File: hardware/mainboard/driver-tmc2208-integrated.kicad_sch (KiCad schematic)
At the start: 11 parts, among them M1 JST XH, U7 TMC2208-LA

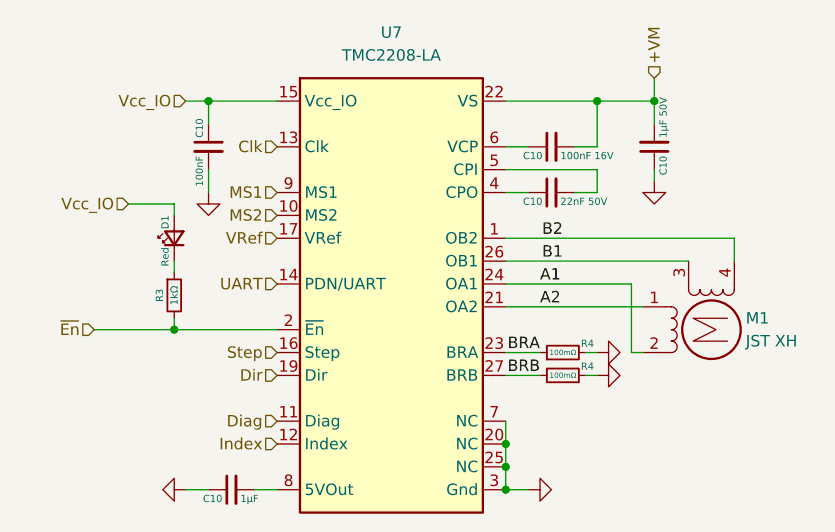
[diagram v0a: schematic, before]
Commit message: this is immediately before i switch the terminus USB hub with the corechips
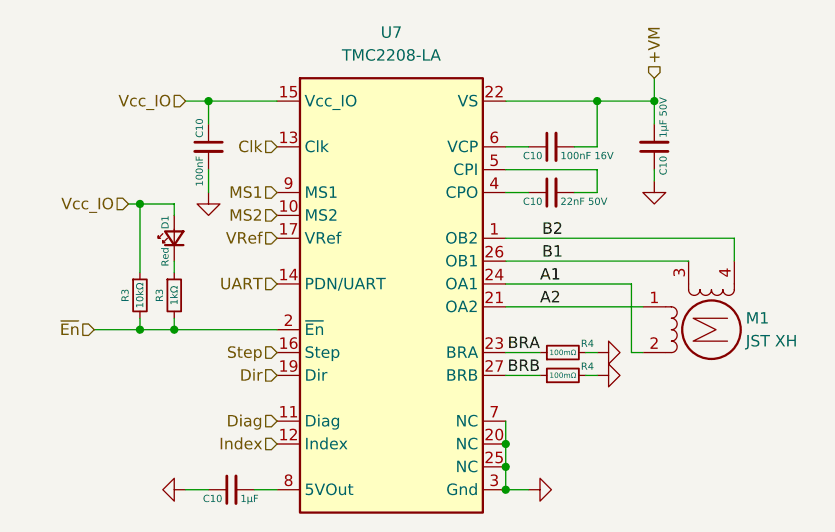
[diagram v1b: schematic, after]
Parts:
- added R3: 10kΩ, AlphaLib:0402R, symbol Device:R_Small
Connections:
- net Vcc_IO: now also R3.1
- net ~{En}: now also R3.2
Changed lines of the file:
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@@
   (junction (at 88.9 39.37) (diameter 0) (color 0 0 0 0)
   )
+  (junction (at 31.75 64.77) (diameter 0) (color 0 0 0 0)
+  )
   (junction (at 82.55 39.37) (diameter 0) (color 0 0 0 0)
   )
@@
   (junction (at 72.39 82.55) (diameter 0) (color 0 0 0 0)
   )
+  (junction (at 31.75 50.8) (diameter 0) (color 0 0 0 0)
+  )
   (wire (pts (xy 72.39 49.53) (xy 74.93 49.53))
     (stroke (width 0) (type default))
@@
     (stroke (width 0) (type default))
   )
+  (wire (pts (xy 31.75 50.8) (xy 31.75 58.42))
+    (stroke (width 0) (type default))
+  )
   (wire (pts (xy 97.79 54.61) (xy 97.79 57.15))
     (stroke (width 0) (type default))
@@
     (stroke (width 0) (type default))
   )
+  (wire (pts (xy 31.75 64.77) (xy 35.56 64.77))
+    (stroke (width 0) (type default))
+  )
   (wire (pts (xy 39.37 39.37) (xy 46.99 39.37))
     (stroke (width 0) (type default))
   )
+  (wire (pts (xy 31.75 50.8) (xy 35.56 50.8))
+    (stroke (width 0) (type default))
+  )
   (wire (pts (xy 72.39 39.37) (xy 82.55 39.37))
     (stroke (width 0) (type default))
@@
     (stroke (width 0) (type default))
   )
+  (wire (pts (xy 31.75 63.5) (xy 31.75 64.77))
+    (stroke (width 0) (type default))
+  )
   (wire (pts (xy 72.39 77.47) (xy 72.39 80.01))
     (stroke (width 0) (type default))
@@
     (stroke (width 0) (type default))
   )
-  (wire (pts (xy 26.67 64.77) (xy 35.56 64.77))
+  (wire (pts (xy 26.67 64.77) (xy 31.75 64.77))
     (stroke (width 0) (type default))
   )
@@
     (stroke (width 0) (type default))
   )
-  (wire (pts (xy 30.48 50.8) (xy 35.56 50.8))
+  (wire (pts (xy 30.48 50.8) (xy 31.75 50.8))
     (stroke (width 0) (type default))
   )
@@
         )
       )
+    )
+  )
+  (symbol (lib_id "Device:R_Small") (at 31.75 60.96 0) (unit 1)
+    (in_bom yes) (on_board yes) (dnp no)
+    (property "Reference" "R3" (at 30.12 60.96 90)
+      (effects (font (size 0.8 0.8)))
+    )
+    (property "Value" "10kΩ" (at 31.75 60.96 90)
+      (effects (font (size 0.8 0.8)))
+    )
+    (property "Footprint" "AlphaLib:0402R" (at 31.75 60.96 0)
+      (effects (font (size 1.27 1.27)) hide)
+    )
+    (property "Datasheet" "~" (at 31.75 60.96 0)
+      (effects (font (size 1.27 1.27)) hide)
+    )
+    (pin "1")
+    (pin "2")
+    (instances
+      (project "driver-tmc5160"
+        (path "/03364e55-5655-494a-997e-0cd456c2d9b5"
+          (reference "R3") (unit 1)
+        )
+      )
+      (project "mainboard"
+        (path "/1a565782-f217-442e-b118-196625f31c53"
+          (reference "R96") (unit 1)
+        )
+        (path "/1a565782-f217-442e-b118-196625f31c53/956ffa88-460c-45ff-bb37-d040d3cbedfe"
+          (reference "R70") (unit 1)
+        )
+        (path "/1a565782-f217-442e-b118-196625f31c53/28340924-2d90-4a87-bb0b-10ef0633a541"
+          (reference "R71") (unit 1)
+        )
+        (path "/1a565782-f217-442e-b118-196625f31c53/f514cf63-1394-4014-821a-69b4627909f9"
+          (reference "R72") (unit 1)
+        )
+        (path "/1a565782-f217-442e-b118-196625f31c53/6adaba86-2614-4e1b-b3d6-74260a2c85fe"
+          (reference "R67") (unit 1)
+        )
+        (path "/1a565782-f217-442e-b118-196625f31c53/09bb4a8f-8694-4b82-8e1f-fabe3bd11ec7"
+          (reference "R98") (unit 1)
+        )
+        (path "/1a565782-f217-442e-b118-196625f31c53/d34aeff3-da22-4edc-92e0-1591d6117dbc"
+          (reference "R99") (unit 1)
+        )
+        (path "/1a565782-f217-442e-b118-196625f31c53/972ca71f-1c40-4278-8cb4-2b520c3e8975"
+          (reference "R97") (unit 1)
+        )
+        (path "/1a565782-f217-442e-b118-196625f31c53/99778979-7977-44ff-ba7b-f489010f8682"
+          (reference "R100") (unit 1)
+        )
+        (path "/1a565782-f217-442e-b118-196625f31c53/f6e6a5bb-7803-4b0b-883d-433919711a15"
+          (reference "R102") (unit 1)
+        )
+        (path "/1a565782-f217-442e-b118-196625f31c53/64a332d7-9292-493c-af4b-24f0e80d7999"
+          (reference "R105") (unit 1)
+        )
+      )

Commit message: added more 3D models and created first few renders
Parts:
- M1: footprint corevus:XKB_X8821WR-04S -> corevus:JST_XH_1x04-Side
- U7: footprint Package_DFN_QFN:TQFN-28-1EP_5x5mm_P0.5mm_EP3.25x3.25mm_ThermalVias -> corevus:TMC220x
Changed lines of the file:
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@@
       (effects (font (size 1.27 1.27)))
     )
-    (property "Footprint" "Package_DFN_QFN:TQFN-28-1EP_5x5mm_P0.5mm_EP3.25x3.25mm_ThermalVias" (at 58.42 87.63 0)
+    (property "Footprint" "corevus:TMC220x" (at 58.42 87.63 0)
       (effects (font (size 1.27 1.27)) hide)
     )
@@
       (effects (font (size 1.27 1.27)) (justify right))
     )
-    (property "Footprint" "corevus:XKB_X8821WR-04S" (at 95.504 65.024 0)
-      (effects (font (size 1.27 1.27)) hide)
-    )
+    (property "Footprint" "corevus:JST_XH_1x04-Side" (at 95.504 65.024 0)
+      (effects (font (size 1.27 1.27)) hide)
+    )
